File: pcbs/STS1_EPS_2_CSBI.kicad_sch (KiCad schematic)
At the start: 2 parts

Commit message: Finished first revision of schematic.
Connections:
- net EPS_ANT_DEPLOY: now reaches CSBI_2.23 (Pin_23)
- net EPS_CHARGING: no longer names the net of CSBI_2.25 (Pin_25), CSBI_2.26 (Pin_26)
- no-connect marks 15 -> 16
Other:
- moved on the sheet: CSBI_2

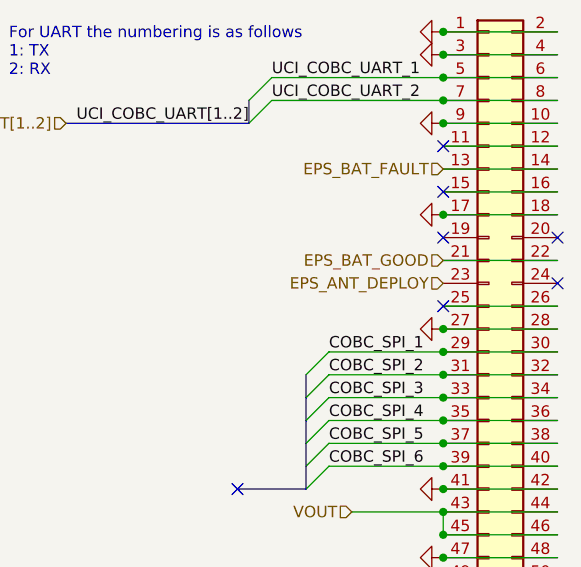
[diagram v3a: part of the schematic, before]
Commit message: Cleared all DRC errors of STS1_EPS_1.
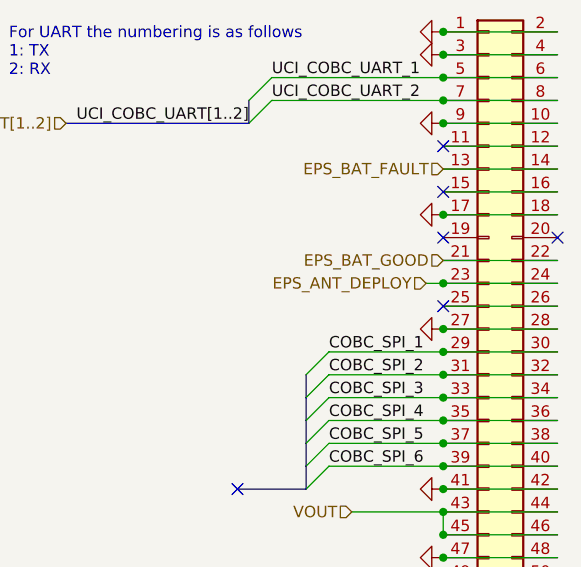
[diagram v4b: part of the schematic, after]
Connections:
- net EPS_ANT_DEPLOY: now also CSBI_2.24 (Pin_24)
- no-connect marks 16 -> 15
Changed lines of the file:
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@@
   (junction (at 193.04 48.26) (diameter 0) (color 0 0 0 0)
+  )
+  (junction (at 193.04 71.12) (diameter 0) (color 0 0 0 0)
   )
   (junction (at 87.63 102.87) (diameter 0) (color 0 0 0 0)
@@
   (no_connect (at 87.63 90.17))
   (no_connect (at 87.63 87.63))
-  (no_connect (at 205.74 71.12))
   (bus_entry (at 177.8 93.98) (size 2.54 -2.54)
     (stroke (width 0) (type default) (color 0 0 0 0))
@@
     (stroke (width 0) (type default) (color 0 0 0 0))
   )
+  (wire (pts (xy 191.135 71.12) (xy 193.04 71.12))
+    (stroke (width 0) (type default) (color 0 0 0 0))
+  )
   (bus (pts (xy 177.8 83.82) (xy 177.8 86.36))
     (stroke (width 0) (type default) (color 0 0 0 0))
@@
   )
   (wire (pts (xy 193.04 50.8) (xy 205.74 50.8))
+    (stroke (width 0) (type default) (color 0 0 0 0))
+  )
+  (wire (pts (xy 193.04 71.12) (xy 205.74 71.12))
     (stroke (width 0) (type default) (color 0 0 0 0))
   )
@@
     (effects (font (size 1.27 1.27)) (justify left bottom))
   )
-  (hierarchical_label "EPS_ANT_DEPLOY" (shape input) (at 193.04 71.12 180)
+  (hierarchical_label "EPS_ANT_DEPLOY" (shape input) (at 191.135 71.12 180)
     (effects (font (size 1.27 1.27)) (justify right))
   )

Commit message: Worked on STS1_EPS_2.
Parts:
- added H1, H2, H3, H4: MountingHole_Pad, MountingHole:MountingHole_4.3mm_M4_Pad_Via, symbol Mechanical:MountingHole_Pad
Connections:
- net GND: now also H1.1, H2.1, H3.1, H4.1
- net COBC_SPI_1: no longer names the net of CSBI_2.29 (Pin_29), CSBI_2.30 (Pin_30)
- net COBC_SPI_2: no longer names the net of CSBI_2.31 (Pin_31), CSBI_2.32 (Pin_32)
- net COBC_SPI_3: no longer names the net of CSBI_2.33 (Pin_33), CSBI_2.34 (Pin_34)
- net COBC_SPI_4: no longer names the net of CSBI_2.35 (Pin_35), CSBI_2.36 (Pin_36)
- net COBC_SPI_5: no longer names the net of CSBI_2.37 (Pin_37), CSBI_2.38 (Pin_38)
- net COBC_SPI_6: no longer names the net of CSBI_2.39 (Pin_39), CSBI_2.40 (Pin_40)
- net EDU_SPI_1: no longer names the net of CSBI_1.21 (Pin_21), CSBI_1.22 (Pin_22)
- net EDU_SPI_2: no longer names the net of CSBI_1.19 (Pin_19), CSBI_1.20 (Pin_20)
- net EDU_SPI_3: no longer names the net of CSBI_1.17 (Pin_17), CSBI_1.18 (Pin_18)
- net EDU_SPI_4: no longer names the net of CSBI_1.15 (Pin_15), CSBI_1.16 (Pin_16)
- net EDU_SPI_5: no longer names the net of CSBI_1.13 (Pin_13), CSBI_1.14 (Pin_14)
- net EDU_SPI_6: no longer names the net of CSBI_1.11 (Pin_11), CSBI_1.12 (Pin_12)
- net UART_COBC_EDU_1: no longer names the net of CSBI_1.45 (Pin_45), CSBI_1.46 (Pin_46)
- net UART_COBC_EDU_2: no longer names the net of CSBI_1.43 (Pin_43), CSBI_1.44 (Pin_44)
- no-connect marks 15 -> 5
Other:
- note removed: "For SPI Buses the numbering is as follows 1: CLK 2: MOSI 3: MISO 4: CS1 5: CS2 ........"
